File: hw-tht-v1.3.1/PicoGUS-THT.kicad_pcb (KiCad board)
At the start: 2 copper layers, 103.7 x 99.8 mm, 88 parts, among them J1 IRQDMA_JP, J10 GY-PCM5102, J11 USB-A, J3 Bus_ISA_8bit, J5 SJ1-3535NG, J6 UART_TX, J7 USB power jumper, J8 SJ1-3535NG-GR, J9 Waveblaster, U1 Pico, U10 74AHCT126, U11 NE5532, U12 USBLC6-2SC6, U2 74AHC244, U3 SN74CB3T3257, U4 SN74CB3T3257, U5 74AHC14, U6 74AHC00, U7 74AHC00, U8 APS6404L-3SQR-SN, U9 PCM5100A

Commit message: THT rev B: U9 CPVDD cap, U12 flow-through at J11, wide GND strap for finger B10
- C36 (new, 0.1 uF X7R 0603, Yageo CC0603KRX7R9BB104 / LCSC C14663 basic part) right under U9 pins 1-3:
  CPVDD -> C36 -> CPGND loop ~6.6 mm (before: nearest +3V3 cap C4 23.6 mm of track away). C16 0.5 mm left,
  R7 0.4 mm down, CPGND via below C36, two GND stitching vias for the front pour west of U9. Schematic
  (audio sheet), BOM and DigiKey uploads updated; CPVDD stays on +3V3 as on v1.2/v1.3.0.
- U12 (USBLC6-2SC6) moved right behind J11 and wired flow-through (no stubs; was 13/26 mm), GND via at
  pin 2, VBUS via to J11.1; C35 below U12, C34 0.2 mm up; USB pair re-routed and re-locked (42.2/42.5 mm,
  matched to 0.28 mm); ~RIOR, ~SPI_CS, SPI_RX re-routed locally; board-level pin-1 dot for U12.
- GND finger B10: 1.5-3 mm B.Cu strap into the U3/U4 pour (link 12.6 -> 3.5 mOhm; B10 to U3/U4 GND
  21/18 -> 11/8 mOhm).
- README: the three changes, U12/C36 assembly notes.

DRC with schematic parity: 0 errors, 0 unconnected; ERC 0 errors. No audio net has another net within 0.5 mm.

Co-Authored-By: Claude Opus 5.5 <noreply@anthropic.com>
Claude-Session: https://claude.ai/code/session_011utN3x8yYUNDvkpGCEq5yD
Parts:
- added C36: 0.1uF, Capacitor_SMD:C_0603_1608Metric, F.Cu at (150.4, 71.8)
- moved U12 7.22 mm to (203.8, 90.9)
- moved C35 1.94 mm to (204.4, 94.2), turned to 180 degrees
- moved C16 0.50 mm to (147.3, 72.0)
- moved R7 0.40 mm to (151.3, 74.7)
- moved C34 0.20 mm to (202.3, 84.3)
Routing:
- net USB_DM: track 58.8 -> 42.5 mm
- net /USB host port/VBUS_USB: track 30.7 -> 24.3 mm, vias 1 -> 2
- net GND: track 761.4 -> 756.8 mm, vias 90 -> 93
- net USB_DP: track 45.0 -> 42.2 mm
- net ~{SPI_CS}: track 34.1 -> 36.1 mm
- net ~{RIOR}: track 78.8 -> 80.4 mm
- net Net-(U9-CAPP): track 5.69 -> 6.19 mm

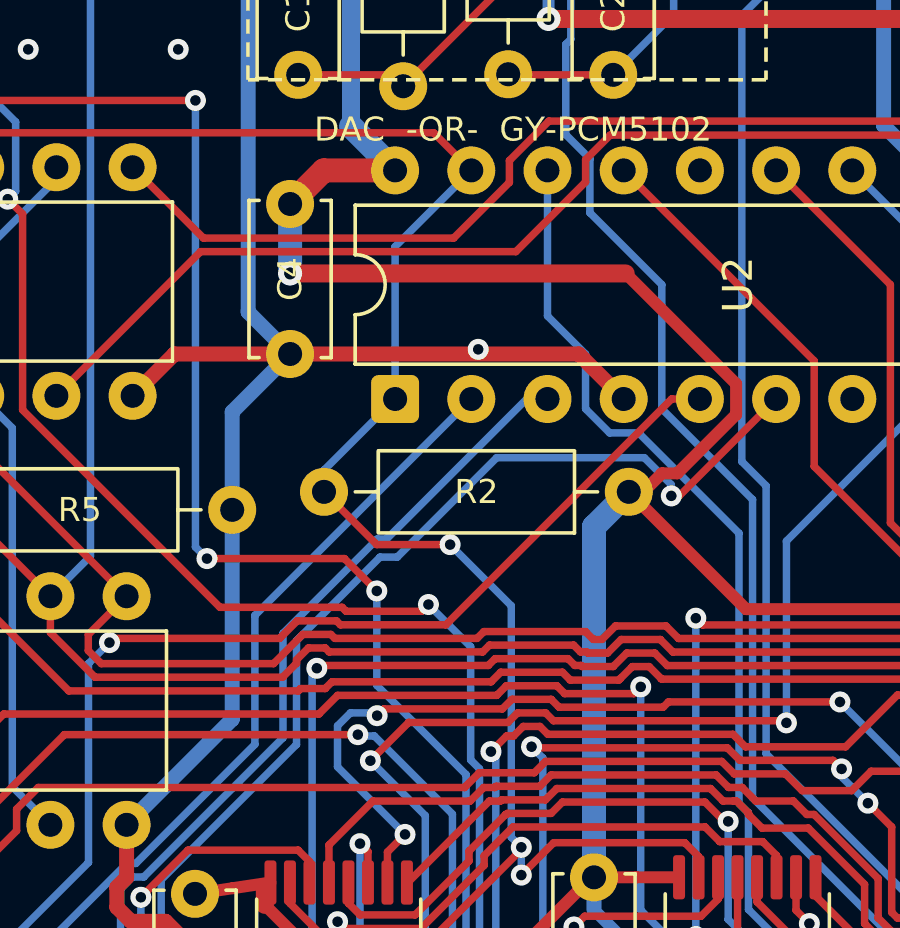
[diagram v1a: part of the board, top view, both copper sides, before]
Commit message: THT rev B: back texts, '< REAR' at the bracket holes, R2 and C4 aligned
- Back version/licence block now ends with 'Thanks to polpo and all the PicoGUS contributors. / The 1.3
  version is dedicated to my wonderful family, Mila and Alisa.'; the separate vertical dedication along the
  far edge is removed (its tribute is now in the block).
- '< REAR' moved 4.79 mm toward the bracket: the arrow tip is in line with the H1/H2 hole centres (x 216.396).
- R2 down 0.6 mm onto the R5/R6 line (y 99.0); TC's back-side diagonal shifted 0.34 mm to clear its pad.
- C4 0.27 mm right, in line with C19 (x 147.84).
- Back artwork re-cut around the moved pads; README back-silkscreen paragraph updated.

DRC with schematic parity: 0 errors, 0 unconnected.

Co-Authored-By: Claude Opus 5.5 <noreply@anthropic.com>
Claude-Session: https://claude.ai/code/session_011utN3x8yYUNDvkpGCEq5yD
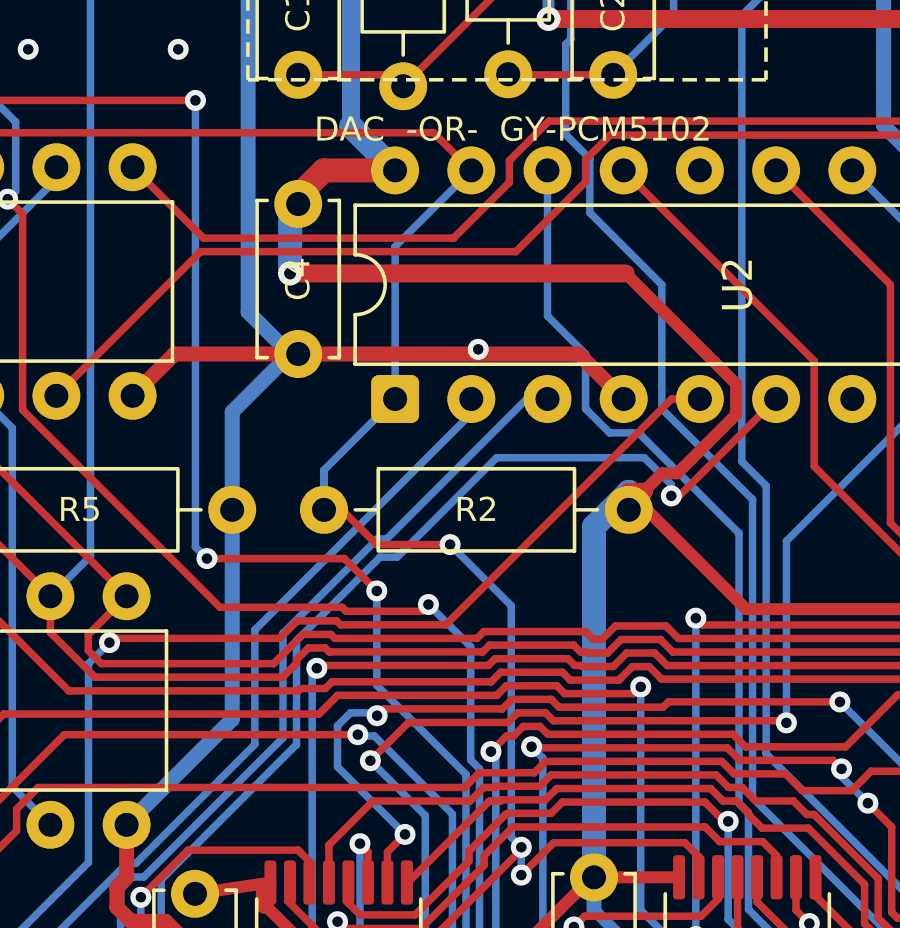
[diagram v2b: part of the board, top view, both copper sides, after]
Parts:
- moved R2 0.60 mm to (158.9, 99.0)
- moved C4 0.27 mm to (147.8, 88.8)
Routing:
- net +3V3: track 355.0 -> 360.4 mm
- net ~{BUSOE}: track 82.9 -> 86.7 mm
- net GND: track 756.8 -> 757.9 mm
- net TC: track 48.2 -> 48.9 mm
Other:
- board text added: "PicoGUS v1.3.1 © 2023-2026 Ian Scott (polpo), Vidar Waagbø (waagbo) Licensed under CERN-OHL-P v2 https://github.com/waagbo/picogus Thanks to polpo and all the PicoGUS contributors. The 1.3 version is dedicated to my wonderful family, Mila and Alisa."
- board text removed: "PicoGUS v1.3.1 © 2023-2026 Ian Scott (polpo), Vidar Waagbø (waagbo) Licensed under CERN-OHL-P v2 https://github.com/waagbo/picogus Thanks to all the people that have contributed over the years!"
- board text removed: "This version is dedicated to Mila and Alisa, my two wonderful princesses, who fill my world with joy."

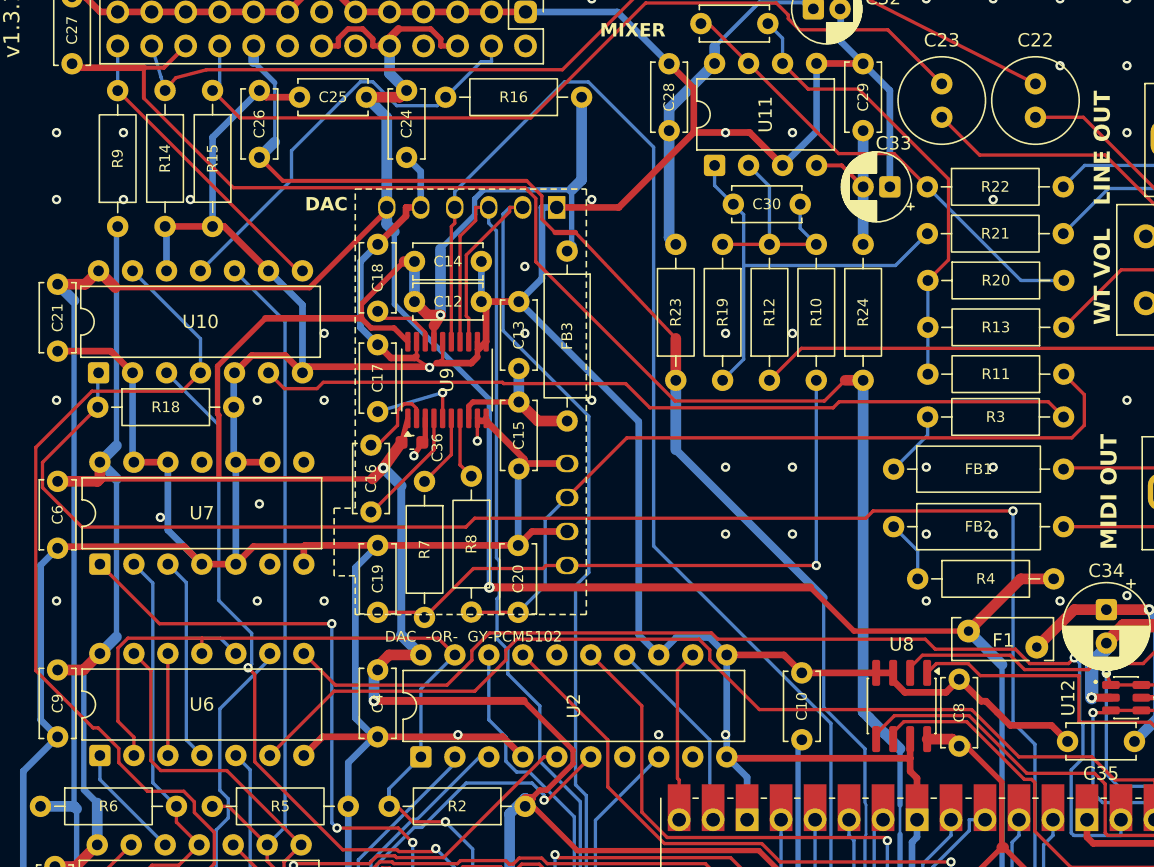
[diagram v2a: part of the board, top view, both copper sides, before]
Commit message: THT rev B: DAC area 1 mm toward the rear
The GY-PCM5102 module outline (J10), U9 and its parts (C12-C20, C36, FB3, R7, R8), their routing and the two
DAC texts move 1.0 mm up, so the 'DAC -OR- GY-PCM5102' heading has 1.1 mm of air above U2's pins (was
0.13 mm). Tracks crossing the area edge bend at 45 degrees or slide along their lines; +12V hops over C24's
GND pad (C24 then joins GND on B.Cu only); one GND stitching via ties the new front ground strip under the
heading. Back artwork re-cut. Audio coupling, I2S/MIDI spacings, the C36 loop and the +-12V widths unchanged.

DRC with schematic parity: 0 errors, 0 unconnected; same warning classes and silkscreen counts as before.

Co-Authored-By: Claude Opus 5.5 <noreply@anthropic.com>
Claude-Session: https://claude.ai/code/session_011utN3x8yYUNDvkpGCEq5yD
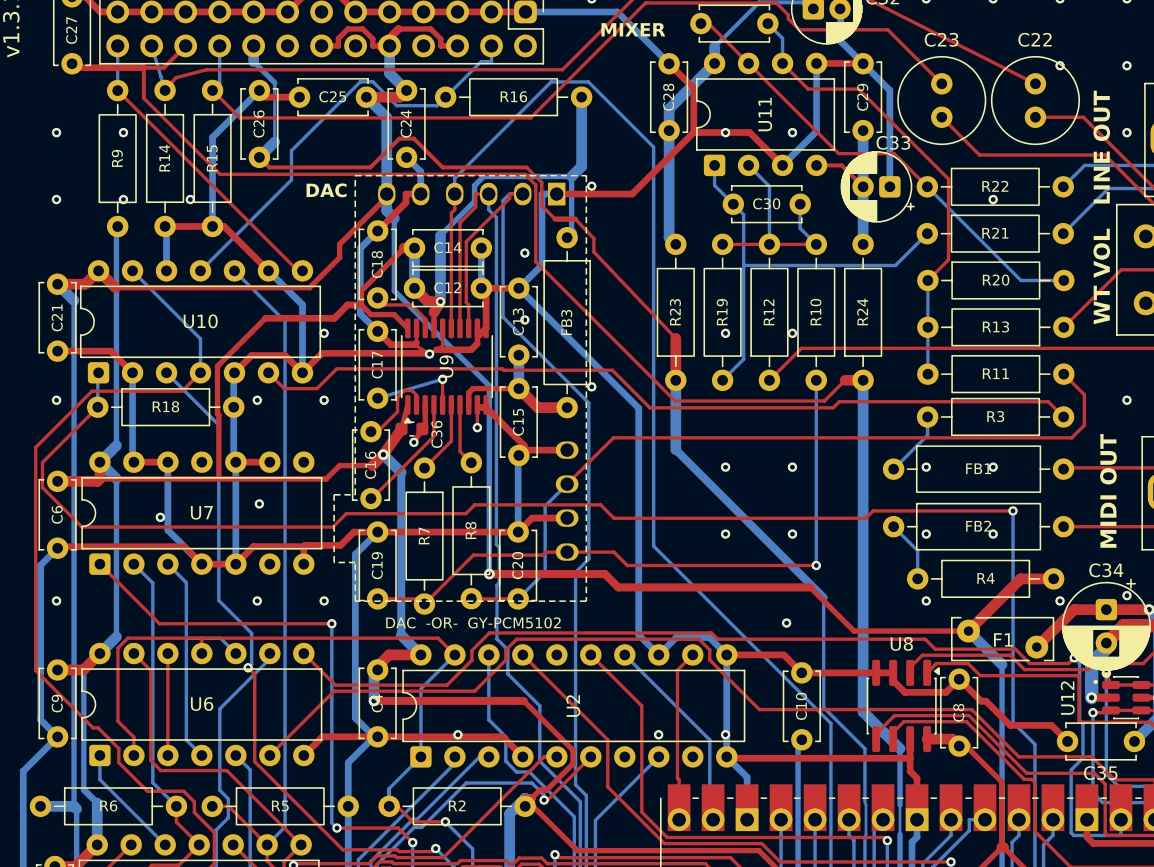
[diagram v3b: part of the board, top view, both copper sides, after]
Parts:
- moved C12 1.00 mm to (155.6, 60.3)
- moved C13 1.00 mm to (158.4, 60.3)
- moved C14 1.00 mm to (155.6, 57.3)
- moved C15 1.00 mm to (158.4, 67.8)
- moved C16 1.00 mm to (147.3, 71.0)
- moved C17 1.00 mm to (147.8, 68.5)
- moved C18 1.00 mm to (147.8, 61.0)
- moved C19 1.00 mm to (147.8, 78.5)
- moved C20 1.00 mm to (158.3, 78.5)
- moved C36 1.00 mm to (150.4, 70.8)
- moved FB3 1.00 mm to (162.0, 56.5)
- moved J10 1.00 mm to (154.0, 68.2)
- moved R7 1.00 mm to (151.3, 73.7)
- moved R8 1.00 mm to (154.8, 73.3)
- moved U9 1.00 mm to (153.0, 66.1)
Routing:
- net +12V: track 126.5 -> 128.8 mm
- net GND: track 757.9 -> 759.3 mm, vias 93 -> 94
- net DIN: track 81.1 -> 82.1 mm
- net BCK: track 84.5 -> 85.5 mm
- net +3V3: track 360.4 -> 361.2 mm
- net Net-(R3-Pad1): track 61.6 -> 62.4 mm
- net ~{RI/OCHRDY}: track 126.6 -> 127.4 mm
- net -12V: track 149.9 -> 150.5 mm
